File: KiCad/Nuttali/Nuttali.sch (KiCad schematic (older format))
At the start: 1 part

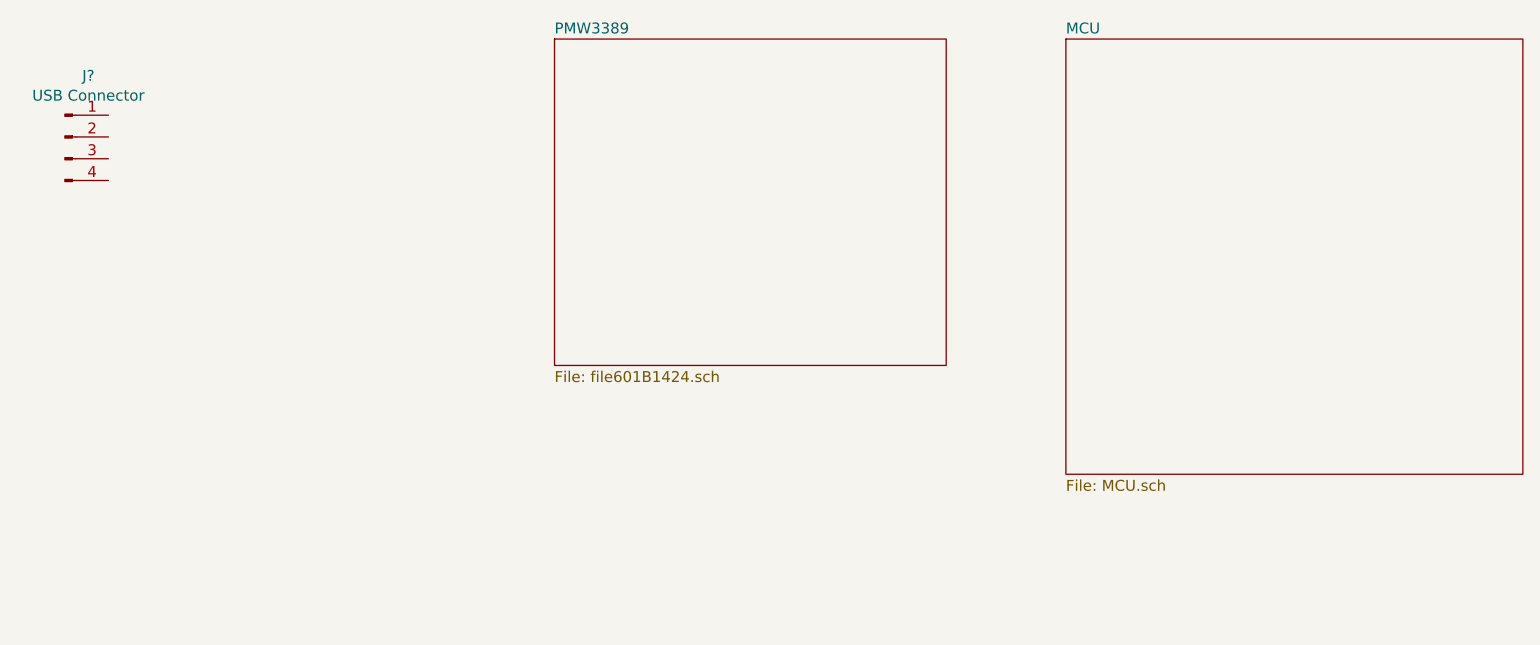
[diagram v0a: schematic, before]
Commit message: Small changes on PMW
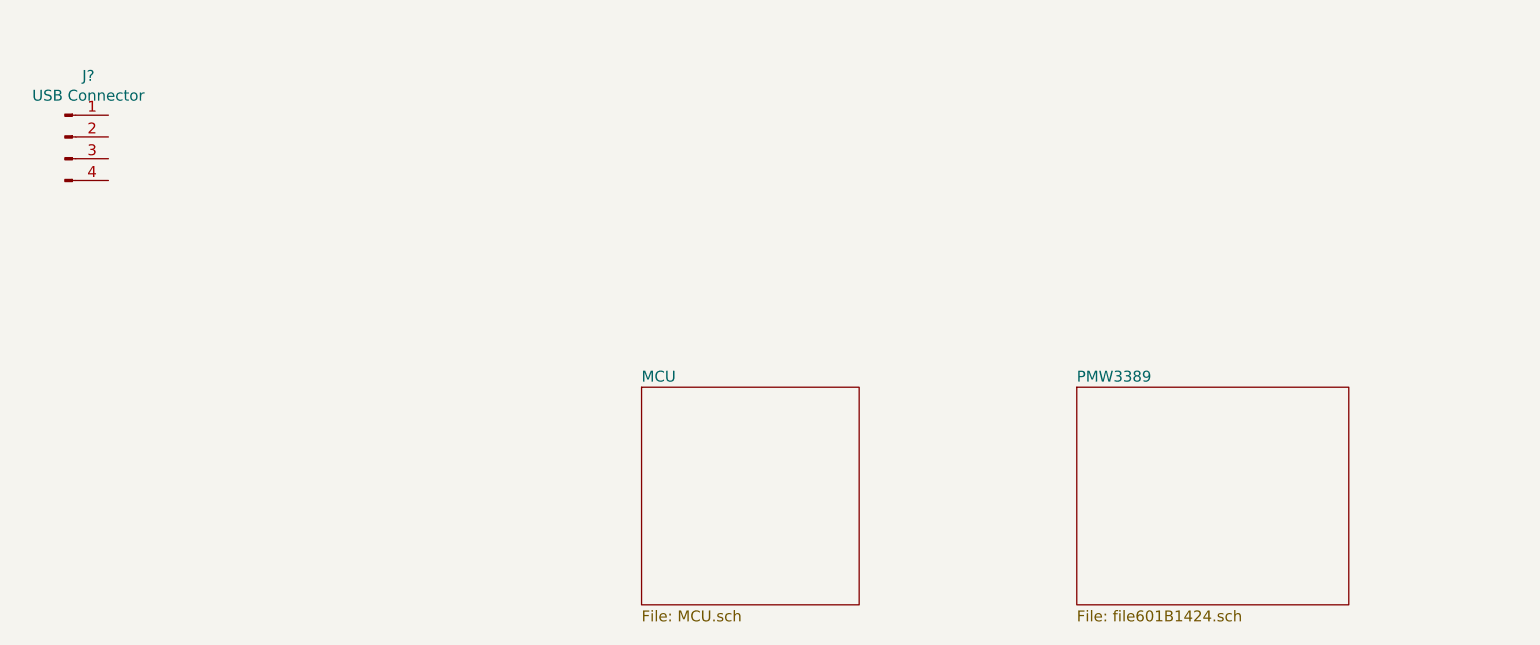
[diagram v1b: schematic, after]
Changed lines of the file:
@@
 $EndComp
 $Sheet
-S 6950 900  2100 2000
+S 5000 2500 1000 1000
 U 6022F0F9
 F0 "MCU" 50
@@
 $EndSheet
 $Sheet
-S 4600 900  1800 1500
+S 7000 2500 1250 1000
 U 601B1425
 F0 "PMW3389" 50

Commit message: Fixed MCU
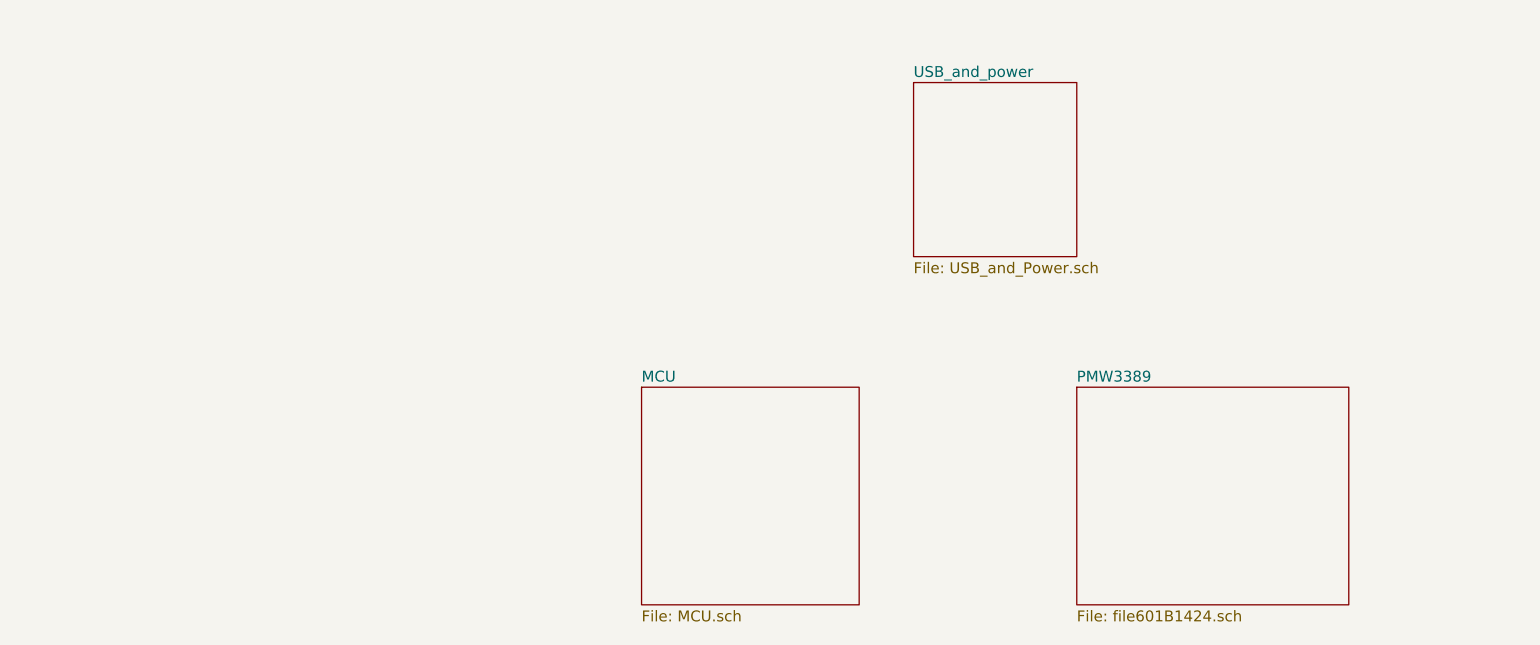
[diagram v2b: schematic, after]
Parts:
- removed J?: USB Connector, symbol Connector:Conn_01x04_Male
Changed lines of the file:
@@
 $Descr A4 11693 8268
 encoding utf-8
-Sheet 1 3
+Sheet 1 4
 Title ""
 Date ""
@@
 Comment4 ""
 $EndDescr
-$Comp
-L Connector:Conn_01x04_Male J?
-U 1 1 601B0A84
-P 2350 1350
-F 0 "J?" H 2458 1631 50  0000 C CNN
-F 1 "USB Connector" H 2458 1540 50  0000 C CNN
-F 2 "" H 2350 1350 50  0001 C CNN
-F 3 "~" H 2350 1350 50  0001 C CNN
-	1    2350 1350
-	1    0    0    -1
-$EndComp
 $Sheet
 S 5000 2500 1000 1000
@@
 F1 "file601B1424.sch" 50
 $EndSheet
+$Sheet
+S 6250 1100 750  800
+U 601D470C
+F0 "USB_and_power" 50
+F1 "USB_and_Power.sch" 50
+$EndSheet
 $EndSCHEMATC
